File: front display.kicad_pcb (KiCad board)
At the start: 2 copper layers, 165.1 x 57.1 mm, 6 parts, among them P1 CONN_02X14

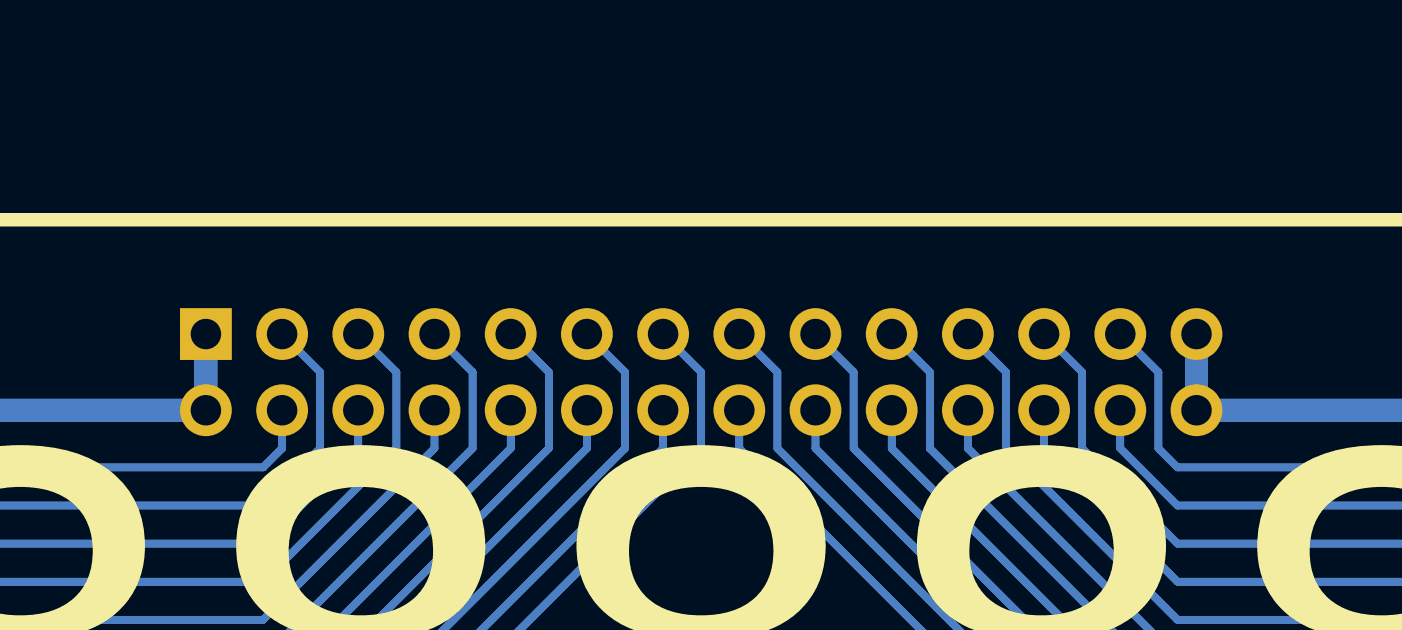
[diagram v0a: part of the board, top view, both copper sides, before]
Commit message: Connector position change and layout fix.
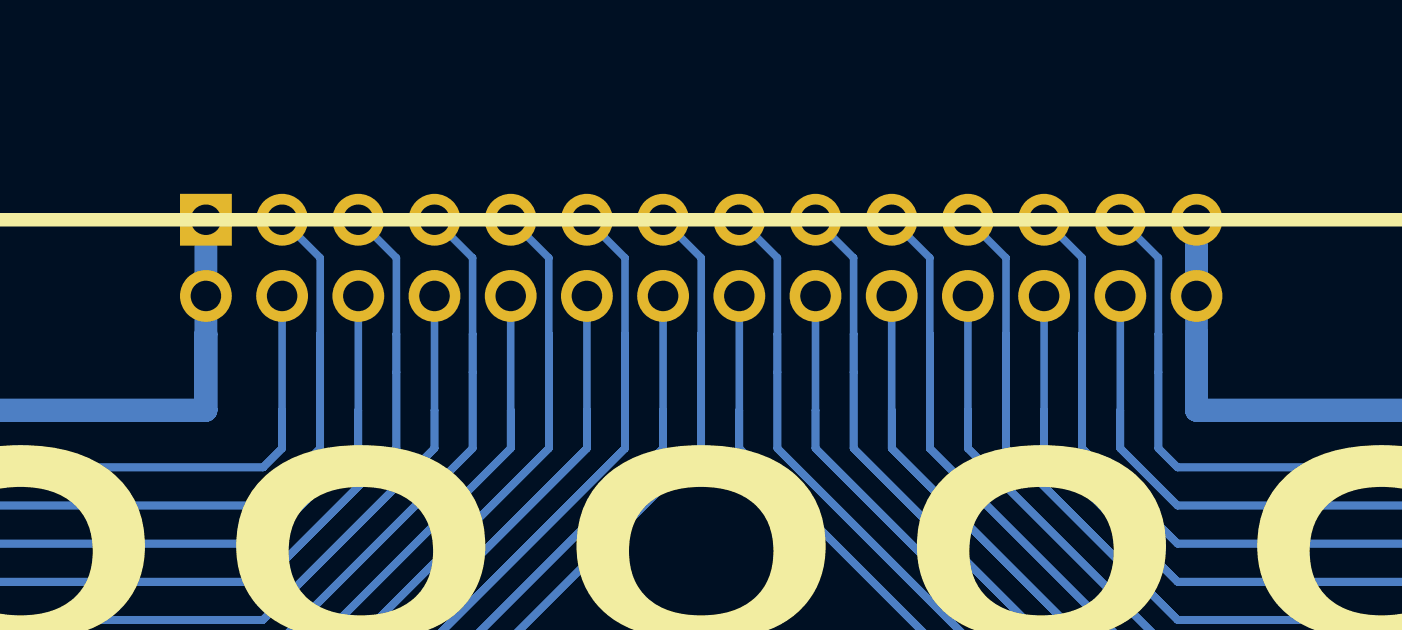
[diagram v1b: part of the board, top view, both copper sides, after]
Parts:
- moved P1 3.81 mm to (132.1, 85.1)
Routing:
- net Net-(DISP1-Pad26): track 138.0 -> 144.4 mm
- net Net-(DISP1-Pad8): track 119.2 -> 123.0 mm
- net Net-(DISP1-Pad6): track 124.3 -> 128.1 mm
- net Net-(DISP1-Pad4): track 129.3 -> 133.1 mm
- net Net-(DISP1-Pad24): track 129.3 -> 133.1 mm
- net Net-(DISP1-Pad20): track 119.2 -> 123.0 mm
- net Net-(DISP1-Pad2): track 134.4 -> 138.2 mm
- net Net-(DISP1-Pad18): track 114.1 -> 117.9 mm
- net Net-(DISP1-Pad16): track 109.0 -> 112.8 mm
- net Net-(DISP1-Pad14): track 103.9 -> 107.7 mm
- net Net-(DISP1-Pad12): track 109.0 -> 112.8 mm
- net Net-(DISP1-Pad10): track 114.1 -> 117.9 mm
- net Net-(DISP1-Pad1): track 138.3 -> 142.1 mm
- net Net-(DISP1-Pad22): track 124.3 -> 128.1 mm
- net Net-(DISP1-Pad3): track 138.0 -> 141.3 mm
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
